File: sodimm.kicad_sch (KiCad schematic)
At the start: 5 parts, among them J201 SODIMM-260

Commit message: jk im stupid forgot to route the flash
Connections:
- net GND: no longer J201.212, J201.216
- new net HOLD: J201.216
- new net WRITE_PROT: J201.212
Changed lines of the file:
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@@
 	(wire
 		(pts
+			(xy 323.85 165.1) (xy 334.01 165.1)
+		)
+		(stroke
+			(width 0)
+			(type default)
+		)
+	)
+	(wire
+		(pts
 			(xy 288.29 205.74) (xy 288.29 203.2)
 		)
@@
 	(wire
 		(pts
+			(xy 323.85 160.02) (xy 334.01 160.02)
+		)
+		(stroke
+			(width 0)
+			(type default)
+		)
+	)
+	(wire
+		(pts
 			(xy 58.42 48.26) (xy 58.42 45.72)
 		)
@@
 		)
 	)
+	(hierarchical_label "HOLD"
+		(shape input)
+		(at 334.01 165.1 0)
+		(effects
+			(font
+				(size 1.27 1.27)
+			)
+			(justify left)
+		)
+	)
 	(hierarchical_label "PA"
 		(shape bidirectional)
@@
 		)
 	)
+	(hierarchical_label "WRITE_PROT"
+		(shape input)
+		(at 334.01 160.02 0)
+		(effects
+			(font
+				(size 1.27 1.27)
+			)
+			(justify left)
+		)
+	)
 	(hierarchical_label "VDDUSB"
 		(shape input)
@@
 	(symbol
 		(lib_id "power:GND")
-		(at 323.85 160.02 90)
-		(unit 1)
-		(exclude_from_sim no)
-		(in_bom yes)
-		(on_board yes)
-		(dnp no)
-		(fields_autoplaced yes)
-		(property "Reference" "#PWR0285"
-			(at 330.2 160.02 0)
-			(effects
-				(font
-					(size 1.27 1.27)
-				)
-				(hide yes)
-			)
-		)
-		(property "Value" "GND"
-			(at 327.66 160.0199 90)
-			(effects
-				(font
-					(size 1.27 1.27)
-				)
-				(justify right)
-			)
-		)
-		(property "Footprint" ""
-			(at 323.85 160.02 0)
-			(effects
-				(font
-					(size 1.27 1.27)
-				)
-				(hide yes)
-			)
-		)
-		(property "Datasheet" ""
-			(at 323.85 160.02 0)
-			(effects
-				(font
-					(size 1.27 1.27)
-				)
-				(hide yes)
-			)
-		)
-		(property "Description" "Power symbol creates a global label with name \"GND\" , ground"
-			(at 323.85 160.02 0)
-			(effects
-				(font
-					(size 1.27 1.27)
-				)
-				(hide yes)
-			)
-		)
-		(pin "1"
-		)
-		(instances
-			(project "DU UC V1 - Minnow"
-				(path "/0aeff2df-21bc-4c76-95d6-83ff8577a8db/d936cc52-813e-4316-9119-269cdeafd53b"
-					(reference "#PWR0285")
-					(unit 1)
-				)
-			)
-		)
-	)
-	(symbol
-		(lib_id "power:GND")
 		(at 107.95 66.04 90)
 		(unit 1)
@@
 					(unit 1)
 				)
-			)
-		)
-	)
-	(symbol
-		(lib_id "power:GND")
-		(at 323.85 165.1 90)
-		(unit 1)
-		(exclude_from_sim no)
-		(in_bom yes)
-		(on_board yes)
-		(dnp no)
-		(fields_autoplaced yes)
-		(property "Reference" "#PWR0287"
-			(at 330.2 165.1 0)
-			(effects
-				(font
-					(size 1.27 1.27)
-				)
-				(hide yes)
-			)
-		)
-		(property "Value" "GND"
-			(at 327.66 165.0999 90)
-			(effects
-				(font
-					(size 1.27 1.27)
-				)
-				(justify right)
-			)
-		)
-		(property "Footprint" ""
-			(at 323.85 165.1 0)
-			(effects
-				(font
-					(size 1.27 1.27)
-				)
-				(hide yes)
-			)
-		)
-		(property "Datasheet" ""
-			(at 323.85 165.1 0)
-			(effects
-				(font
-					(size 1.27 1.27)
-				)
-				(hide yes)
-			)
-		)
-		(property "Description" "Power symbol creates a global label with name \"GND\" , ground"
-			(at 323.85 165.1 0)
-			(effects
-				(font
-					(size 1.27 1.27)
-				)
-				(hide yes)
-			)
-		)
-		(pin "1"
-		)
-		(instances
-			(project "DU UC V1 - Minnow"
-				(path "/0aeff2df-21bc-4c76-95d6-83ff8577a8db/d936cc52-813e-4316-9119-269cdeafd53b"
-					(reference "#PWR0287")
-					(unit 1)
-				)

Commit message: fixed like a bunch of things, power and new xcvr and lights and other goodies, also started layout
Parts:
- J201: footprint Connector_PCBEdge:SODIMM-260_DDR4_H4.0-5.2_OrientationStd_Socket -> bfr_connectors:SODIMM-260 DDR4
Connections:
- net GND: now also C201.1, C202.1, J201.11, J201.13, J201.15, J201.17, J201.19, J201.209, J201.213, J201.217, J201.221, J201.225, J201.229, J201.233, J201.237, J201.249, J201.250, J201.256, J201.258, J201.260; no longer J201.211, J201.215, J201.219, J201.220, J201.222, J201.223, J201.227, J201.231, J201.235, J201.239, J201.255, J201.257, J201.259
- net GNDPWR: no longer C201.1, C202.1, J201.11, J201.13, J201.15, J201.17, J201.19
- net PA0: now also J201.142; no longer J201.55
- net PA1: now also J201.138; no longer J201.59
- net PA10: now also J201.127; no longer J201.95
- net PA15: now also J201.131; no longer J201.99
- net PA2: now also J201.134; no longer J201.63
- net PA3: now also J201.130; no longer J201.67
- net PA4: now also J201.126; no longer J201.71
- net PA5: now also J201.122; no longer J201.75
- net PA6: now also J201.118; no longer J201.79
- net PA7: now also J201.114; no longer J201.83
- net PA8: now also J201.119; no longer J201.87
- net PA9: now also J201.123; no longer J201.91
- net PB0: now also J201.110; no longer J201.103
- net PB1: now also J201.106; no longer J201.54
- net PB10: now also J201.34; no longer J201.86
- net PB11: now also J201.30; no longer J201.90
- net PB13: now also J201.27; no longer J201.94
- net PB14: now also J201.31; no longer J201.98
- net PB15: now also J201.35; no longer J201.102
- net PB2: now also J201.102; no longer J201.58
- net PB4: now also J201.191; no longer J201.62
- net PB5: now also J201.195; no longer J201.66
- net PB6: now also J201.199; no longer J201.70
- net PB7: now also J201.203; no longer J201.74
- net PB8: now also J201.207; no longer J201.78
- net PB9: now also J201.211; no longer J201.82
- net PC0: now also J201.158; no longer J201.107
- net PC1: now also J201.154; no longer J201.111
- net PC10: now also J201.107; no longer J201.139
- net PC11: now also J201.111; no longer J201.143
- net PC12: now also J201.115; no longer J201.147
- net PC13: now also J201.206; no longer J201.151
- net PC2: now also J201.150; no longer J201.115
- net PC3: now also J201.146; no longer J201.119
- net PC6: now also J201.91; no longer J201.123
- net PC7: now also J201.95; no longer J201.127
- net PC8: now also J201.99; no longer J201.131
- net PC9: now also J201.103; no longer J201.135
- net PD0: now also J201.135; no longer J201.155
- net PD1: now also J201.139; no longer J201.106
- net PD10: now also J201.47; no longer J201.142
- net PD11: now also J201.51; no longer J201.146
- net PD12: now also J201.55; no longer J201.150
- net PD13: now also J201.59; no longer J201.154
- net PD14: now also J201.63; no longer J201.159
- net PD15: now also J201.67; no longer J201.163
- net PD2: now also J201.143; no longer J201.110
- net PD3: now also J201.147; no longer J201.114
- net PD4: now also J201.151; no longer J201.118
- net PD5: now also J201.155; no longer J201.122
- net PD6: now also J201.159; no longer J201.126
- net PD7: now also J201.163; no longer J201.130
- net PD8: now also J201.39; no longer J201.134
- net PD9: now also J201.43; no longer J201.138
- net PE0: now also J201.215; no longer J201.178
- net PE1: now also J201.219; no longer J201.182
- net PE10: now also J201.58; no longer J201.217
- net PE11: now also J201.54; no longer J201.221
- net PE12: now also J201.50; no longer J201.225
- net PE13: now also J201.46; no longer J201.229
- net PE14: now also J201.42; no longer J201.233
- net PE15: now also J201.38; no longer J201.237
- net PE2: now also J201.223; no longer J201.186
- net PE3: now also J201.227; no longer J201.190
- net PE4: now also J201.231; no longer J201.194
- net PE5: now also J201.235; no longer J201.198
- net PE6: now also J201.239; no longer J201.202
- net PE7: now also J201.70; no longer J201.206
- net PE8: now also J201.66; no longer J201.209
- net PE9: now also J201.62; no longer J201.213
- net PF0: now also J201.202; no longer J201.167
- net PF1: now also J201.198; no longer J201.171
- net PF10: now also J201.162; no longer J201.207
- net PF11: now also J201.98; no longer J201.158
- net PF12: now also J201.94; no longer J201.162
- net PF13: now also J201.90; no longer J201.166
- net PF14: now also J201.86; no longer J201.170
- net PF15: now also J201.82; no longer J201.174
- net PF2: now also J201.194; no longer J201.175
- net PF3: now also J201.190; no longer J201.179
- net PF4: now also J201.186; no longer J201.183
- net PF5: now also J201.182; no longer J201.187
- net PF6: now also J201.178; no longer J201.191
- net PF7: now also J201.174; no longer J201.195
- net PF8: now also J201.170; no longer J201.199
- net PF9: now also J201.166; no longer J201.203
- net PG0: now also J201.78; no longer J201.27
- net PG1: now also J201.74; no longer J201.31
- net PG10: now also J201.171; no longer J201.34
- net PG12: now also J201.175; no longer J201.38
- net PG13: now also J201.179; no longer J201.42
- net PG14: now also J201.183; no longer J201.46
- net PG15: now also J201.187; no longer J201.50
- net PG2: now also J201.71; no longer J201.35
- net PG3: now also J201.75; no longer J201.39
- net PG4: now also J201.79; no longer J201.43
- net PG5: now also J201.83; no longer J201.47
- net PG6: now also J201.87; no longer J201.51
- net PG9: now also J201.167; no longer J201.30
- net VBATT: now also J201.220, J201.222; no longer J201.228, J201.230, J201.232, J201.234
- net VDDIO: now also J201.228, J201.230, J201.232, J201.234; no longer J201.244, J201.246, J201.248, J201.250
- net VDDUSB: no longer J201.249
- net VREF: now also J201.244, J201.246, J201.248; no longer J201.256, J201.258, J201.260
- net 3V3_RAW renamed +5V
- net 5V_RAW renamed 3V3A
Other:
- note added: "1.5A max output"
- note added: "2.5A max input"
- note added: "this missing a few... does it fuck up when update board? shouldnt"

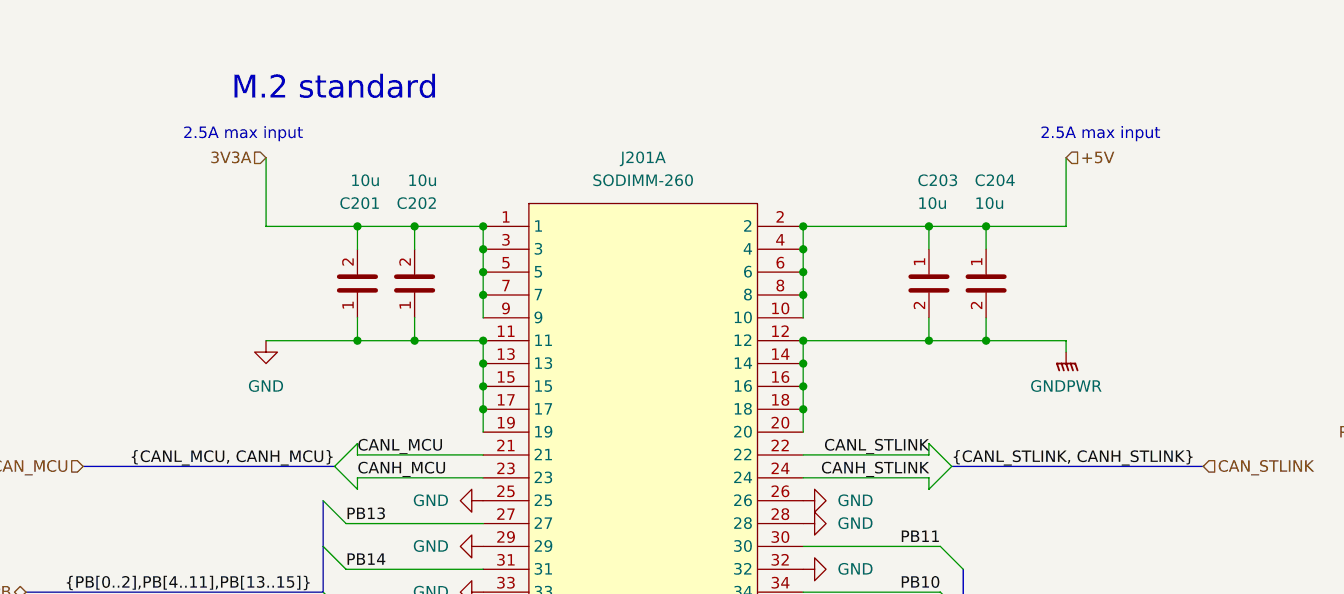
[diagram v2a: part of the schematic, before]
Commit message: quicksave on some R.S. T.S. (mostly layout changes, small pin changes for better routing)
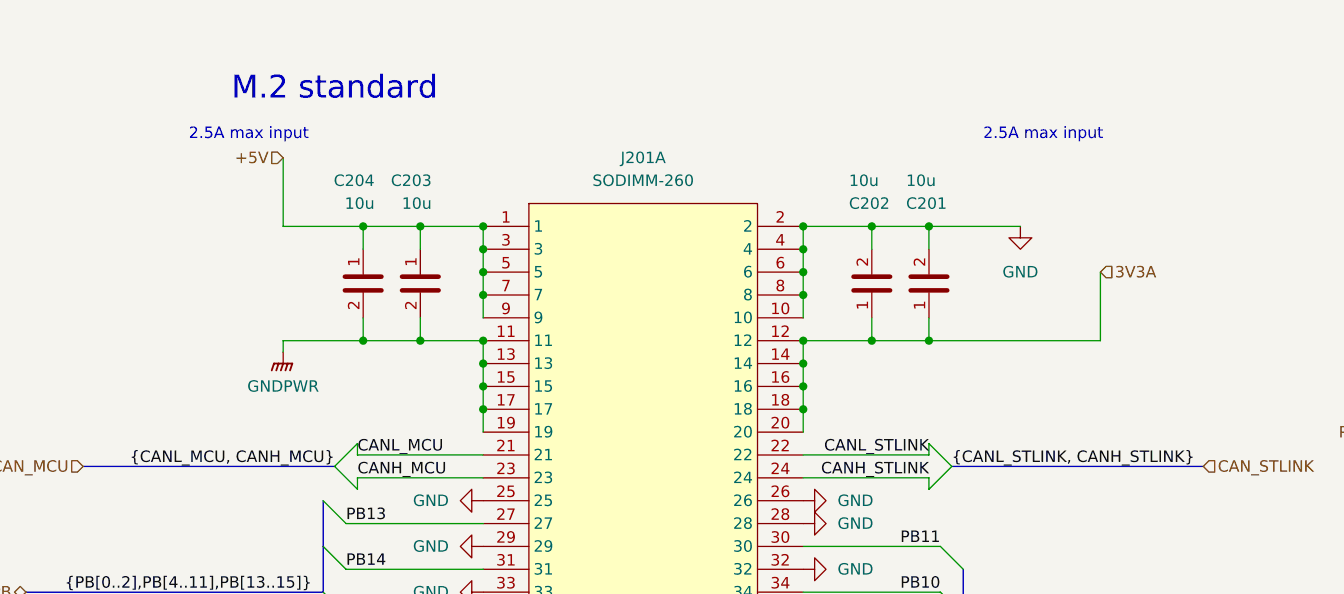
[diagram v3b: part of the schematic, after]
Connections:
- net +5V: now also J201.1, J201.3, J201.5, J201.7, J201.9; no longer J201.10, J201.2, J201.4, J201.6, J201.8
- net 3V3A: now also C201.1, C202.1, J201.12, J201.14, J201.16, J201.18, J201.20; no longer C201.2, C202.2, J201.1, J201.3, J201.5, J201.7, J201.9
- net GND: now also C201.2, C202.2, J201.10, J201.2, J201.4, J201.6, J201.8; no longer C201.1, C202.1, J201.11, J201.13, J201.15, J201.17, J201.19
- net GNDPWR: now also J201.11, J201.13, J201.15, J201.17, J201.19; no longer J201.12, J201.14, J201.16, J201.18, J201.20
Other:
- moved on the sheet: C201, C202, C203, C204

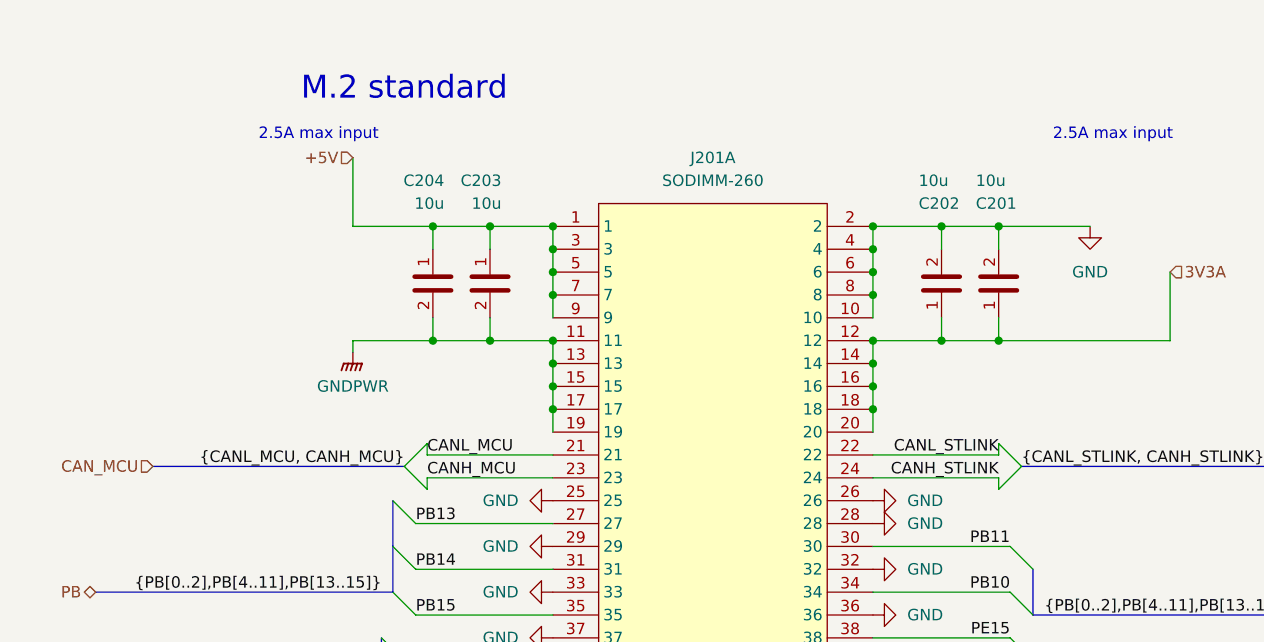
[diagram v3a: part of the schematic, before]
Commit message: laid out most of power, main xcvr, prob some other stuff
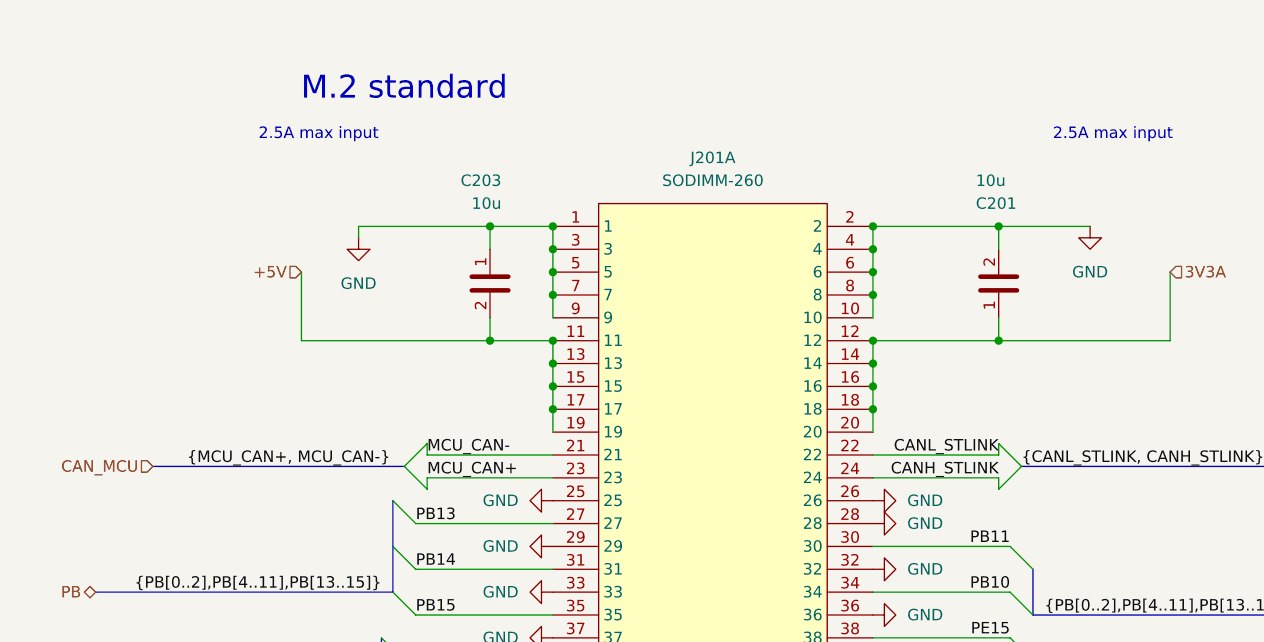
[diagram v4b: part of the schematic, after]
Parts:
- removed C202, C204: 10u, Capacitor_SMD:C_0603_1608Metric_Pad1.08x0.95mm_HandSolder, symbol bfr_capacitors:CL10A106MA8NRNC
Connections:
- net GNDPWR is gone; now on net +5V: C203.2, J201.11, J201.13, J201.15, J201.17, J201.19
- net +5V: no longer C203.1, J201.1, J201.3, J201.5, J201.7, J201.9
- net GND: now also C203.1, J201.1, J201.3, J201.5, J201.7, J201.9
- net CANH_MCU renamed MCU_CAN+
- net CANL_MCU renamed MCU_CAN-

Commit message: i fucken rerouted everything and redid the pinout like 3x, half routed GPIOs
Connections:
- net PA0: now also J201.131; no longer J201.142
- net PA1: now also J201.135; no longer J201.138
- net PA10: now also J201.130; no longer J201.127
- net PA15: now also J201.126; no longer J201.131
- net PA2: now also J201.139; no longer J201.134
- net PA3: now also J201.143; no longer J201.130
- net PA4: now also J201.147; no longer J201.126
- net PA5: now also J201.151; no longer J201.122
- net PA6: now also J201.155; no longer J201.118
- net PA7: now also J201.159; no longer J201.114
- net PA8: now also J201.138; no longer J201.119
- net PA9: now also J201.134; no longer J201.123
- net PB0: now also J201.163; no longer J201.110
- net PB1: now also J201.167; no longer J201.106
- net PB10: now also J201.223; no longer J201.34
- net PB11: now also J201.227; no longer J201.30
- net PB13: now also J201.231; no longer J201.27
- net PB14: now also J201.235; no longer J201.31
- net PB15: now also J201.239; no longer J201.35
- net PB2: now also J201.171; no longer J201.102
- net PB4: now also J201.50; no longer J201.191
- net PB5: now also J201.46; no longer J201.195
- net PB6: now also J201.42; no longer J201.199
- net PB7: now also J201.38; no longer J201.203
- net PB8: now also J201.34; no longer J201.207
- net PB9: now also J201.30; no longer J201.211
- net PC0: now also J201.99; no longer J201.158
- net PC1: now also J201.103; no longer J201.154
- net PC10: now also J201.122; no longer J201.107
- net PC11: now also J201.118; no longer J201.111
- net PC12: now also J201.114; no longer J201.115
- net PC13: now also J201.110; no longer J201.206
- net PC2: now also J201.107; no longer J201.150
- net PC3: now also J201.111; no longer J201.146
- net PC6: now also J201.154; no longer J201.91
- net PC7: now also J201.150; no longer J201.95
- net PC8: now also J201.146; no longer J201.99
- net PC9: now also J201.142; no longer J201.103
- net PD0: now also J201.106; no longer J201.135
- net PD1: now also J201.102; no longer J201.139
- net PD10: now also J201.198; no longer J201.47
- net PD11: now also J201.194; no longer J201.51
- net PD12: now also J201.190; no longer J201.55
- net PD13: now also J201.186; no longer J201.59
- net PD14: now also J201.182; no longer J201.63
- net PD15: now also J201.178; no longer J201.67
- net PD2: now also J201.98; no longer J201.143
- net PD3: now also J201.94; no longer J201.147
- net PD4: now also J201.90; no longer J201.151
- net PD5: now also J201.86; no longer J201.155
- net PD6: now also J201.82; no longer J201.159
- net PD7: now also J201.78; no longer J201.163
- net PD8: now also J201.206; no longer J201.39
- net PD9: now also J201.202; no longer J201.43
- net PE0: now also J201.27; no longer J201.215
- net PE1: now also J201.31; no longer J201.219
- net PE10: now also J201.199; no longer J201.58
- net PE11: now also J201.203; no longer J201.54
- net PE12: now also J201.207; no longer J201.50
- net PE13: now also J201.211; no longer J201.46
- net PE14: now also J201.215; no longer J201.42
- net PE15: now also J201.219; no longer J201.38
- net PE2: now also J201.35; no longer J201.223
- net PE3: now also J201.39; no longer J201.227
- net PE4: now also J201.43; no longer J201.231
- net PE5: now also J201.47; no longer J201.235
- net PE6: now also J201.51; no longer J201.239
- net PE7: now also J201.187; no longer J201.70
- net PE8: now also J201.191; no longer J201.66
- net PE9: now also J201.195; no longer J201.62
- net PF0: now also J201.55; no longer J201.202
- net PF1: now also J201.59; no longer J201.198
- net PF10: now also J201.95; no longer J201.162
- net PF11: now also J201.175; no longer J201.98
- net PF12: now also J201.115; no longer J201.94
- net PF13: now also J201.119; no longer J201.90
- net PF14: now also J201.123; no longer J201.86
- net PF15: now also J201.127; no longer J201.82
- net PF2: now also J201.63; no longer J201.194
- net PF3: now also J201.67; no longer J201.190
- net PF4: now also J201.71; no longer J201.186
- net PF5: now also J201.75; no longer J201.182
- net PF6: now also J201.79; no longer J201.178
- net PF7: now also J201.83; no longer J201.174
- net PF8: now also J201.87; no longer J201.170
- net PF9: now also J201.91; no longer J201.166
- net PG0: now also J201.179; no longer J201.78
- net PG1: now also J201.183; no longer J201.74
- net PG10: now also J201.70; no longer J201.171
- net PG12: now also J201.66; no longer J201.175
- net PG13: now also J201.62; no longer J201.179
- net PG14: now also J201.58; no longer J201.183
- net PG15: now also J201.54; no longer J201.187
- net PG2: now also J201.174; no longer J201.71
- net PG3: now also J201.170; no longer J201.75
- net PG4: now also J201.166; no longer J201.79
- net PG5: now also J201.162; no longer J201.83
- net PG6: now also J201.158; no longer J201.87
- net PG9: now also J201.74; no longer J201.167
- net CANH_STLINK renamed STLINK_CAN+
- net CANL_STLINK renamed STLINK_CAN-

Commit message: holy fucking stupid ass why did u put this upon urself
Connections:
- net GND: now also J201.21, J201.23, J201.259
- net MCU_CAN+: now also J201.257; no longer J201.23
- net MCU_CAN-: now also J201.255; no longer J201.21
